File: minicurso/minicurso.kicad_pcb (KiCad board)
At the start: 2 copper layers, 62.2 x 43.2 mm, 17 parts, among them J1 USB_B_Mini, J2 Conn_01x10, J3 Conn_01x10, J4 Conn_01x06, SW1 SW_Push, U1 ATmega32U4-AU, Y1 16MHz

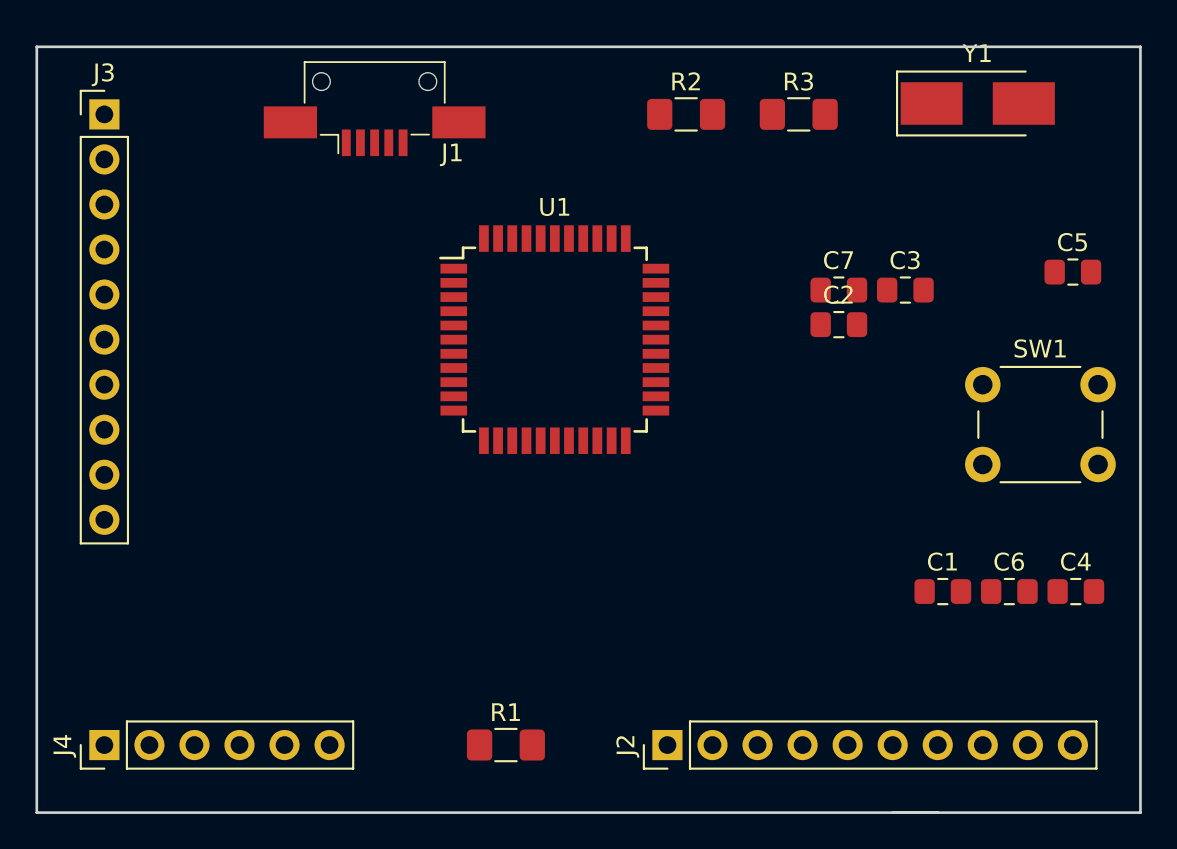
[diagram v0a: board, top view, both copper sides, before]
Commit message: Usando label para facilitar desenho
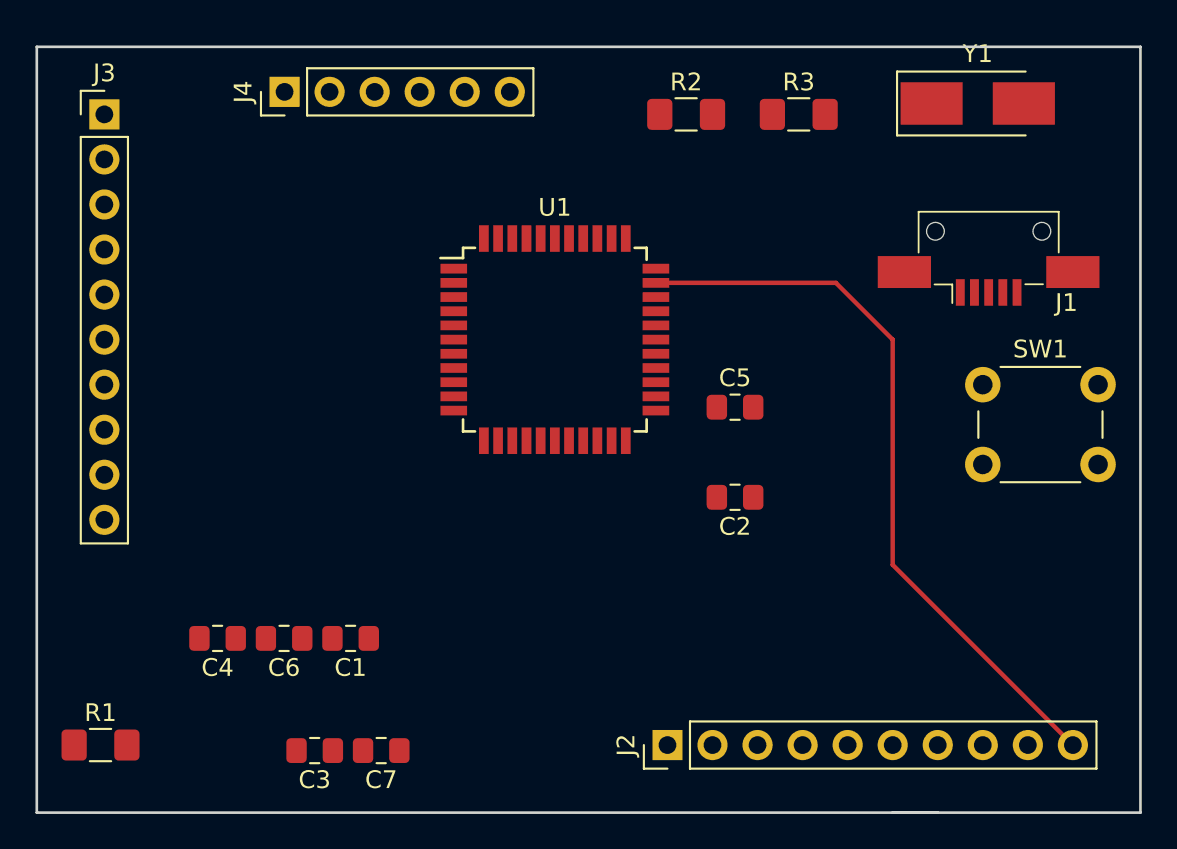
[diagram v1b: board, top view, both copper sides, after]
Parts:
- moved C4 48.5 mm to (67.3, 70.2), turned to 180 degrees
- moved C3 42.2 mm to (72.8, 76.5), turned to 180 degrees
- moved C6 41.0 mm to (71.1, 70.2), turned to 180 degrees
- moved J4 38.2 mm to (71.1, 39.4)
- moved C7 36.6 mm to (76.6, 76.5), turned to 180 degrees
- moved J1 35.6 mm to (110.8, 49.1)
- moved C1 33.5 mm to (74.8, 70.2), turned to 180 degrees
- moved R1 22.9 mm to (60.7, 76.2)
- moved C5 20.5 mm to (96.5, 57.1)
- moved C2 11.4 mm to (96.5, 62.2), turned to 180 degrees
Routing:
- net Net-(J2-Pad10): track 0.00 -> 41.7 mm
- added copper zone on F.Cu, net GND

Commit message: Gerbers files
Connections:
- net Net-(J2-Pad10) renamed Pino32
- net Net-(J2-Pad5) renamed Pino28
- net Net-(J2-Pad6) renamed Pino29
- net Net-(J2-Pad7) renamed Pino30
- net Net-(J2-Pad9) renamed Pino31
- J2 pad 1: Net-(J2-Pad1) -> Pino19
- J2 pad 2: Net-(J2-Pad2) -> Pino20
- J2 pad 3: Net-(J2-Pad3) -> Pino21
- J2 pad 4: Net-(J2-Pad4) -> Pino22
- J2 pad 8: Net-(J2-Pad8) -> Pino12
- J3 pad 1: Net-(J3-Pad1) -> Pino41
- J3 pad 10: Net-(J3-Pad10) -> Pino18
- J3 pad 2: Net-(J3-Pad2) -> Pino1
- J3 pad 3: Net-(J3-Pad3) -> Pino8
- J3 pad 4: Net-(J3-Pad4) -> Pino9
- J3 pad 5: Net-(J3-Pad5) -> Pino10
- J3 pad 6: Net-(J3-Pad6) -> Pino12
- J3 pad 7: Net-(J3-Pad7) -> Pino13
- J3 pad 8: Net-(J3-Pad8) -> Pino16
- J3 pad 9: Net-(J3-Pad9) -> Pino17
- J4 pad 6: Net-(J4-Pad6) -> Pino33
- U1 pad 1: Net-(J3-Pad10) -> Pino1
- U1 pad 10: Net-(J2-Pad3) -> Pino10
- U1 pad 11: Net-(J2-Pad4) -> Pino11
- U1 pad 12: Net-(J2-Pad8) -> Pino12
- U1 pad 18: Net-(J3-Pad1) -> Pino18
- U1 pad 19: Net-(J3-Pad2) -> Pino19
- U1 pad 20: Net-(J3-Pad3) -> Pino20
- U1 pad 21: Net-(J3-Pad4) -> Pino21
- U1 pad 22: Net-(J3-Pad6) -> Pino22
- U1 pad 25: Net-(J3-Pad5) -> Pino25
- U1 pad 26: Net-(J3-Pad7) -> Pino26
- U1 pad 27: Net-(J3-Pad8) -> Pino27
- U1 pad 33: Net-(J3-Pad9) -> Pino33
- U1 pad 36: Net-(J4-Pad6) -> Net-(J4-Pad5)
- U1 pad 37: Net-(J4-Pad5) -> Net-(J4-Pad4)
- U1 pad 38: Net-(J4-Pad4) -> Net-(J4-Pad3)
- U1 pad 39: Net-(J4-Pad3) -> Net-(J4-Pad2)
- U1 pad 40: Net-(J4-Pad2) -> Net-(J4-Pad1)
- U1 pad 41: Net-(J4-Pad1) -> Pino41
- U1 pad 8: Net-(J2-Pad1) -> Pino8
- U1 pad 9: Net-(J2-Pad2) -> Pino9
